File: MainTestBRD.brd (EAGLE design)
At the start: 100 x 80 mm, 24 parts, among them J1 COMPUTER-PERIPHERAL-POWERVERT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, U1 ATMEGA128-SMD

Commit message: intermedate variant
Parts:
- R1, R2: value (none) -> 1.8k; device mbed-rlcq:0.125W -> SparkFun-Resistors:0603-RES
- moved R2 10.2 mm to (86.4, 71.1), turned to 180 degrees
- moved LED2 10.2 mm to (95.2, 71.1)
- flipped J1 to the bottom
- turned R1 to 180 degrees
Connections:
- net N$13 renamed RESET
- net LED1: now also R1.2; no longer R1.P$1
- net LED2: now also R2.2; no longer R2.P$1
- net N$2: now also R2.1; no longer R2.P$2
- net N$5: now also R1.1; no longer R1.P$2
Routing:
- net VCC: track 184.7 -> 30.6 mm
- net GND: track 287.3 -> 240.2 mm
- net PF6: track 22.5 -> 0.00 mm
- net PF4: track 22.5 -> 0.00 mm
- net PF5: track 17.4 -> 0.00 mm
- net LED2: track 37.0 -> 24.7 mm
- net PF7: track 10.9 -> 0.00 mm
- net VDD: track 137.1 -> 128.7 mm
- net N$2: track 2.91 -> 6.55 mm
- net LED1: track 2.98 -> 5.47 mm
- net N$5: track 4.10 -> 6.54 mm
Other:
- board size 100 x 80 mm -> 100 x 62.2 mm

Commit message: other pinouts
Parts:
- removed J1: COMPUTER-PERIPHERAL-POWERVERTICAL, SparkFun-Connectors:COMPUTER-PERIPHERAL-POWER
- removed U$2: JTAGICE3-CONNECTOR100MIL-SMD, con-jtagice3:JTAGICE3-100MIL-SMD
- added JP1: M05X2PTH, SparkFun-Connectors:AVR_ICSP
- added U$3: JTAGICE3-CONNECTOR50MIL-THT, con-jtagice3:JTAGICE3-50MIL
- added U2: (no value), SparkFun-Connectors:USB-AB-MICRO-SMD
- moved R3 45.3 mm to (45.7, 57.1)
- moved R4 43.4 mm to (49.5, 59.7), turned to 270 degrees
- moved LED1 43.0 mm to (52.3, 67.3)
- moved LED2 42.9 mm to (52.3, 69.8)
- moved R1 39.4 mm to (47.0, 67.3)
- moved R2 39.4 mm to (47.0, 69.8)
- moved U$1 38.1 mm to (35.6, 63.5)
- moved C9 37.4 mm to (58.8, 41.2)
- moved C10 36.5 mm to (58.8, 36.4), turned to 0 degrees
- moved U1 36.4 mm to (35.6, 38.1)
- moved S1 35.9 mm to (52.1, 24.1), turned to 270 degrees
- moved Y1 35.6 mm to (51.7, 38.8)
- moved S2 35.6 mm to (20.3, 73.7)
- moved IT1 34.9 mm to (7.62, 71.1)
- moved C2 30.7 mm to (6.35, 38.1), turned to 0 degrees
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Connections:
- new net N$10: JP1.10, U1.6
- new net N$11: JP1.8, U1.5
- new net N$12: JP1.6, U1.4
- new net N$13: JP1.4, U1.3
- new net N$14: JP1.2, U1.2
- new net N$15: JP1.9, U1.7
- new net N$16: JP1.7, U1.8
- new net N$17: JP1.5, U1.9
- new net N$3: R3.1, U1.28
- net BT_RX: no longer R3.1, U1.28
- net GND: now also JP1.3, U$3.P0, U$3.P2, U2.GND; no longer J1.GND
- net PF4: now also U$3.P1; no longer U$2.1
- net PF5: now also U$3.P5; no longer U$2.5
- net PF6: now also U$3.P3; no longer U$2.3
- net PF7: now also U$3.P9; no longer U$2.9
- net VCC: now also JP1.1, U$3.P4, U2.VBUS; no longer J1.5V, U$2.4
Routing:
- net VCC: track 30.6 -> 153.8 mm
- net VDD: track 128.7 -> 89.3 mm
- net RESET: track 46.3 -> 15.7 mm
- net BT_RX: track 35.1 -> 8.97 mm
- net BT_TX: track 41.6 -> 20.4 mm
- net PF7: track 0.00 -> 20.7 mm
- net N$17: track 0.00 -> 20.0 mm
- net N$3: track 0.00 -> 18.2 mm
- net N$16: track 0.00 -> 14.9 mm
- net N$15: track 0.00 -> 9.30 mm
- net PF5: track 0.00 -> 8.82 mm
- net PF6: track 0.00 -> 8.82 mm
- net N$14: track 0.00 -> 7.15 mm
- net N$13: track 0.00 -> 6.27 mm
- net N$10: track 0.00 -> 5.97 mm
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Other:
- board size 100 x 62.2 mm -> 64.4 x 62.3 mm
- board text added: "Vcc"

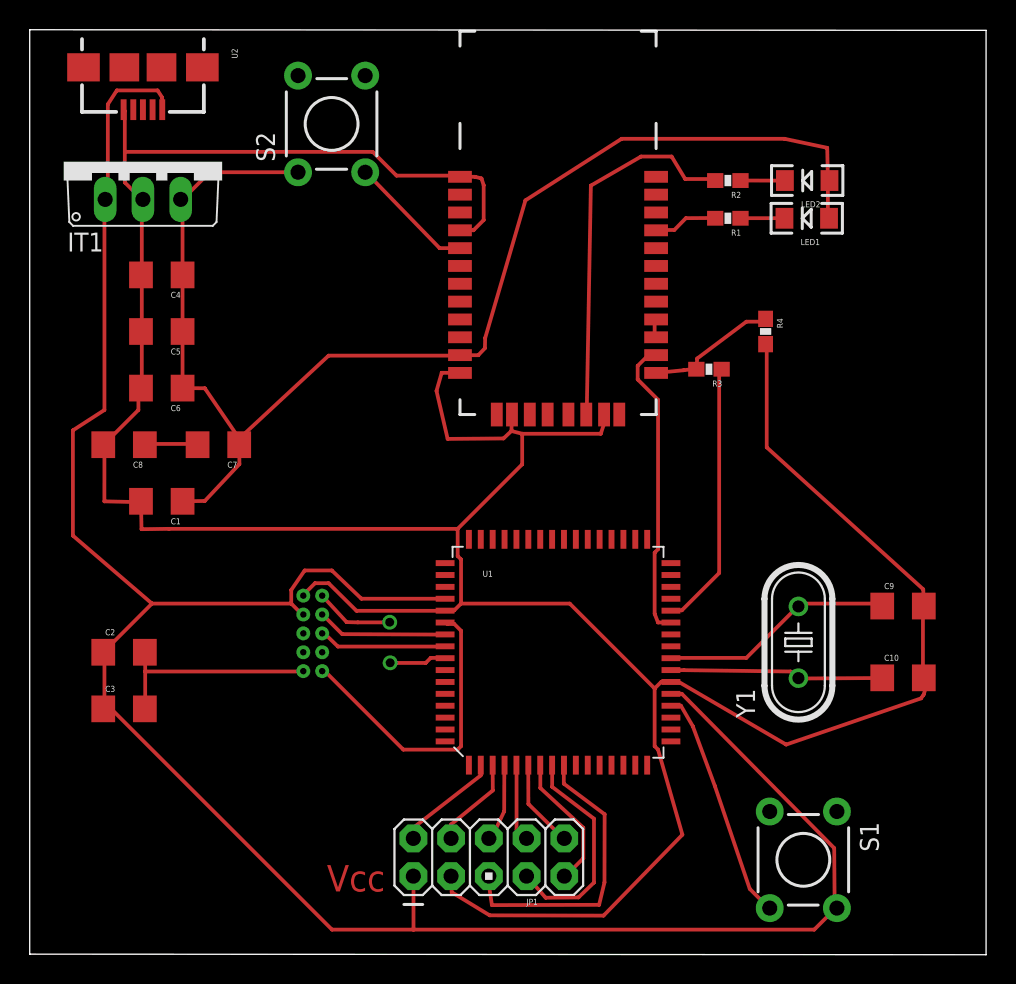
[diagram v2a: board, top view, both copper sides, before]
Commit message: additional pin outs added
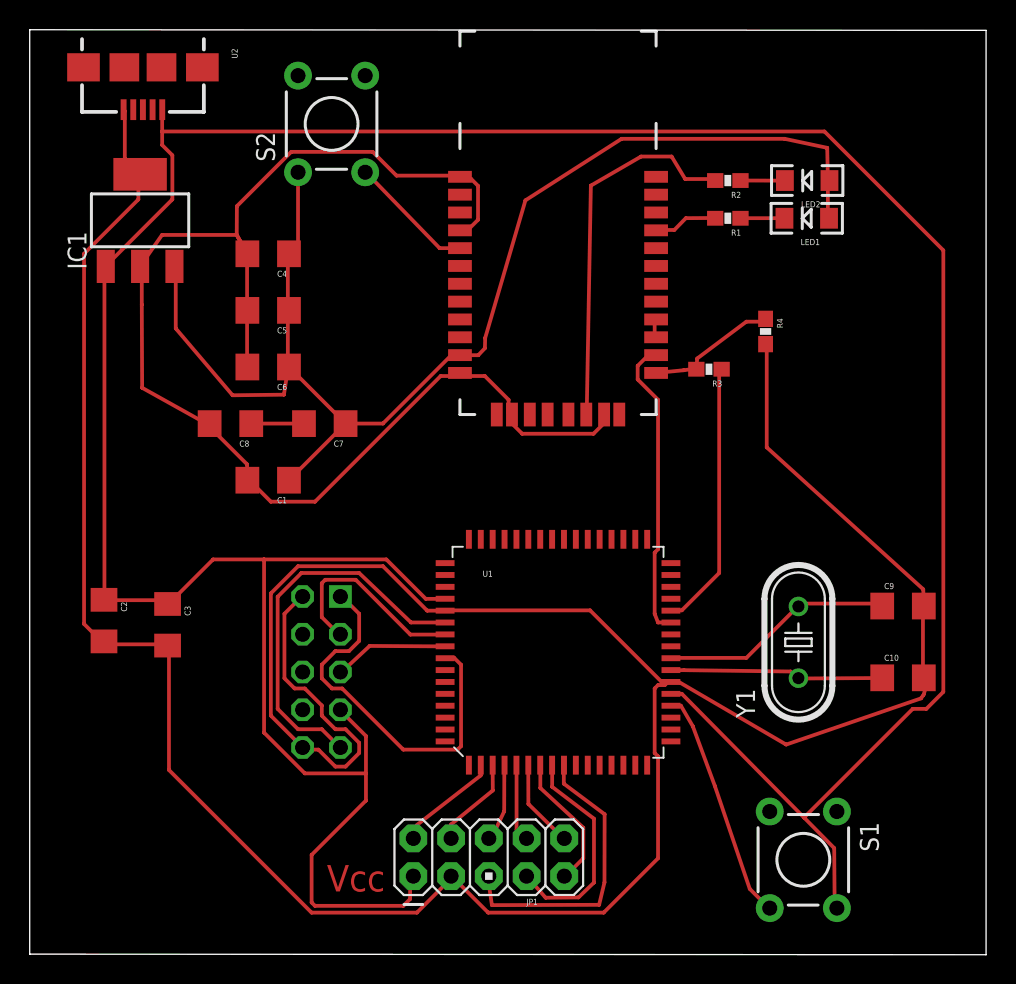
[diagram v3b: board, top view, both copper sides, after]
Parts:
- removed IT1: LM3940IT-3.3, LM3940:TO220V
- removed U$3: JTAGICE3-CONNECTOR50MIL-THT, con-jtagice3:JTAGICE3-50MIL
- added IC1: LM3940IMP-3.3, mylib:SOT223
- added JP2: AVR-JTAG-10, atmel:AVR-JTAG-10
- moved C1 7.30 mm to (16.1, 49.7)
- moved C4 7.30 mm to (16.1, 64.9)
- moved C5 7.30 mm to (16.1, 61.1)
- moved C7 7.30 mm to (19.9, 53.5)
- moved C8 7.30 mm to (13.5, 53.5)
- moved C6 7.30 mm to (16.1, 57.3)
- moved C3 6.37 mm to (9.28, 40.0), turned to 270 degrees
- moved C2 2.52 mm to (5.00, 40.2), turned to 270 degrees
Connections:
- removed net PF4: U$3.P1, U1.57
- removed net PF5: U$3.P5, U1.56
- removed net PF6: U$3.P3, U1.55
- removed net PF7: U$3.P9, U1.54
- new net AGND: C1.2, C4.2, C5.2, C6.2, C8.2, IC1.2, U$1.1, U$1.12, U$1.28, U$1.29, U$1.4
- new net N$18: JP2.3, U1.55
- new net N$19: JP2.9, U1.54
- new net N$6: JP2.1, U1.57
- new net N$9: JP2.5, U1.56
- net GND: now also IC1.4, JP2.10, JP2.2; no longer C1.2, C4.2, C5.2, C6.2, C8.2, IT1.2, U$1.1, U$1.12, U$1.28, U$1.29, U$1.4, U$3.P0, U$3.P2
- net VCC: now also IC1.1, JP2.7; no longer IT1.1, U$3.P4
- net VDD: now also IC1.3; no longer IT1.3
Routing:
- net AGND: track 0.00 -> 92.5 mm
- net VCC: track 153.8 -> 222.0 mm
- net N$19: track 0.00 -> 26.5 mm
- net N$6: track 0.00 -> 25.9 mm, vias 1 -> 0
- net GND: track 235.1 -> 212.5 mm
- net PF7: track 20.7 -> 0.00 mm
- net N$18: track 0.00 -> 13.9 mm
- net PF5: track 8.82 -> 0.00 mm
- net PF6: track 8.82 -> 0.00 mm
- net N$9: track 0.00 -> 7.73 mm, vias 1 -> 0
- net PF4: track 5.29 -> 0.00 mm
- net N$7: track 3.72 -> 0.00 mm
- net VDD: track 89.3 -> 88.1 mm

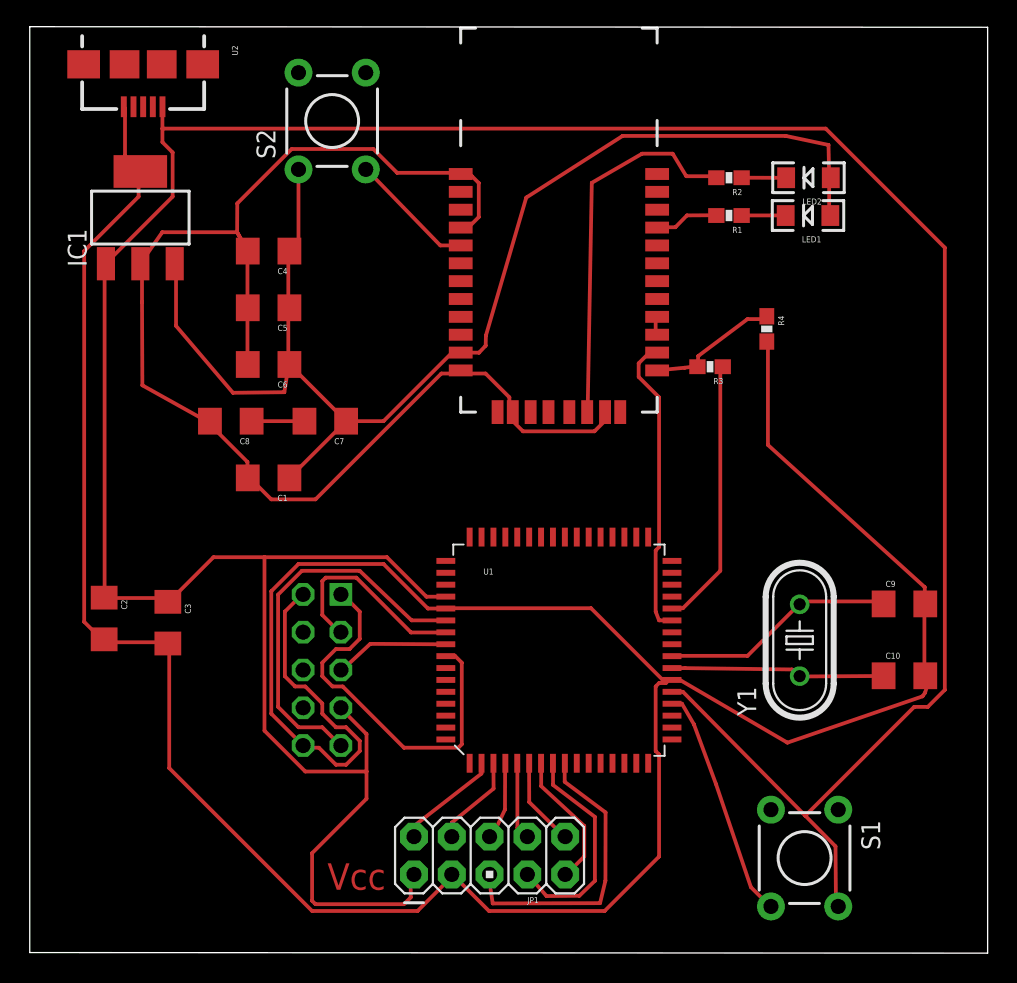
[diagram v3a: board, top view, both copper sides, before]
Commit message: new power led
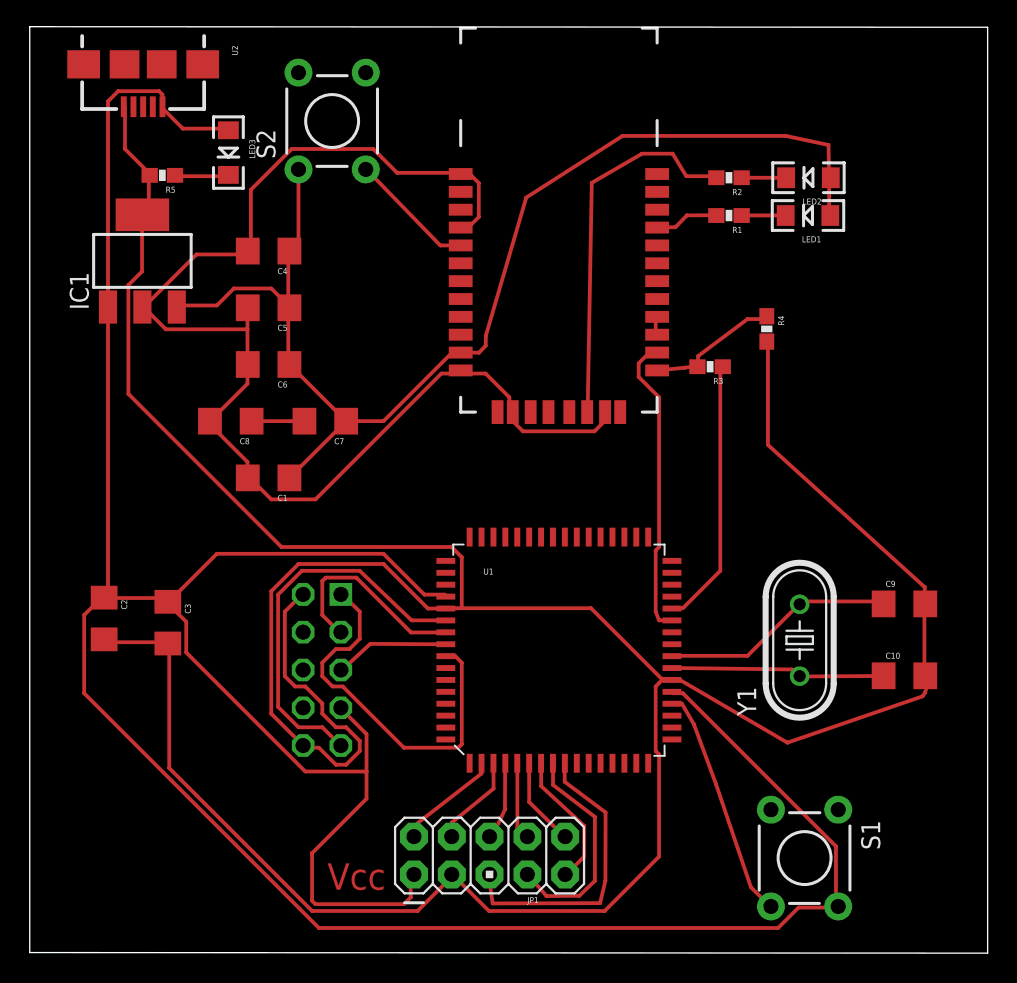
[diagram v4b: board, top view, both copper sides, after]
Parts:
- added LED3: (no value), SparkFun-LED:LED-1206
- added R5: 1.8k, SparkFun-Resistors:0603-RES
- moved IC1 2.91 mm to (3.76, 60.5)
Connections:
- new net N$20: LED3.C, R5.1
- net GND: now also R5.2
- net VCC: now also LED3.A
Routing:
- net VCC: track 222.0 -> 196.6 mm
- net GND: track 212.5 -> 225.1 mm
- net VDD: track 88.1 -> 81.0 mm
- net AGND: track 92.5 -> 87.1 mm
- net N$20: track 0.00 -> 3.65 mm

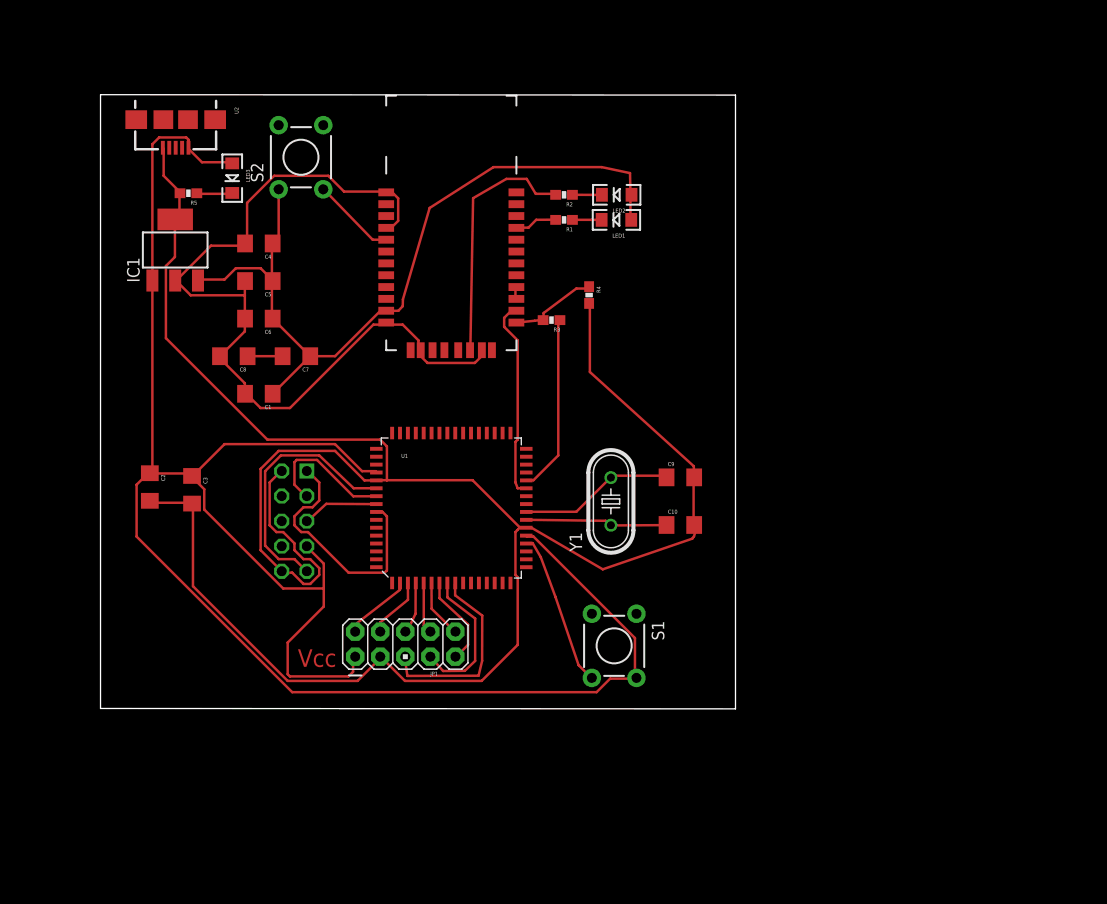
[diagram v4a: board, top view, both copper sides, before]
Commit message: new usb connector
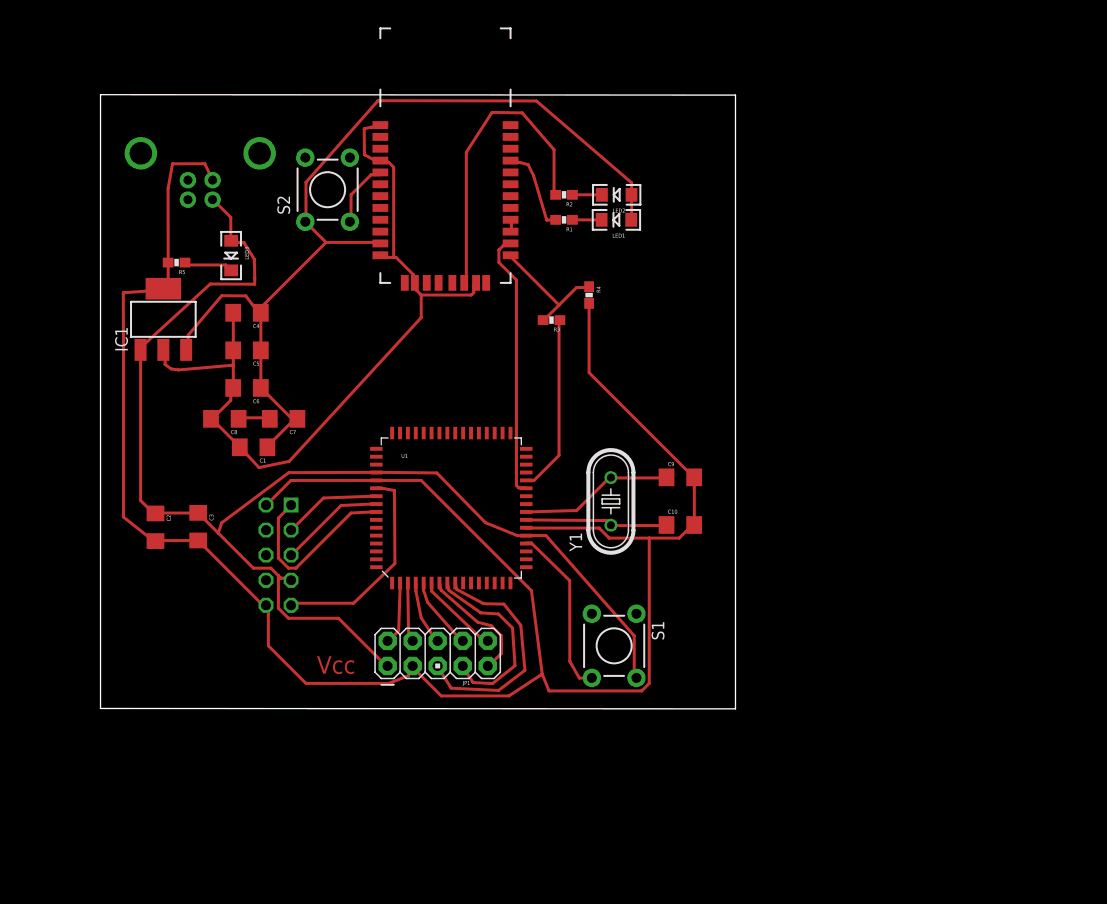
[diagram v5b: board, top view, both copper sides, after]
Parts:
- removed U2: (no value), SparkFun-Connectors:USB-AB-MICRO-SMD
- added JP4: USB-B, SparkFun-Connectors:USB-B-PTH
- moved LED3 7.85 mm to (13.2, 63.7)
- moved R5 7.13 mm to (7.71, 63.0)
- moved C4 7.13 mm to (14.8, 57.9)
- moved C5 7.13 mm to (14.8, 54.1)
- moved IC1 7.13 mm to (2.56, 53.4)
- moved C6 7.13 mm to (14.8, 50.3)
- moved U$1 6.85 mm to (35.0, 70.3)
- moved C7 6.48 mm to (18.6, 47.1)
- moved C8 6.41 mm to (12.6, 47.1)
- moved C1 5.45 mm to (15.5, 44.3)
- moved S2 4.26 mm to (23.0, 70.4)
- moved C2 4.12 mm to (5.57, 36.1)
- moved JP2 3.80 mm to (18.1, 33.3)
- moved C3 3.79 mm to (9.90, 36.2)
- moved JP1 3.41 mm to (34.2, 23.4)
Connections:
- net GND: now also JP4.GND; no longer U2.GND
- net VCC: now also JP4.VBUS; no longer U2.VBUS
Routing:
- net VCC: track 196.6 -> 131.9 mm
- net VDD: track 81.0 -> 94.7 mm
- net GND: track 225.1 -> 212.6 mm
- net N$6: track 25.9 -> 18.6 mm
- net BT_TX: track 20.4 -> 27.2 mm
- net LED2: track 25.2 -> 31.0 mm
- net N$19: track 26.5 -> 21.5 mm
- net LED1: track 4.32 -> 8.76 mm
- net N$16: track 14.9 -> 19.3 mm
- net AGND: track 87.1 -> 82.8 mm
- net BT_RX: track 8.97 -> 13.2 mm
- net N$17: track 20.0 -> 24.0 mm
- net N$18: track 13.9 -> 9.98 mm
- net N$15: track 9.30 -> 12.3 mm
- net N$9: track 7.73 -> 10.7 mm
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
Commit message: __
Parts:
- moved C1 16.5 mm to (28.6, 54.3), turned to 270 degrees
- moved C8 13.8 mm to (25.7, 51.3), turned to 270 degrees
- moved C7 12.4 mm to (25.7, 57.3), turned to 270 degrees
- moved C6 8.41 mm to (22.6, 53.6), turned to 270 degrees
- moved C4 4.30 mm to (15.0, 53.6), turned to 270 degrees
- moved C5 3.95 mm to (18.8, 53.6), turned to 270 degrees
- moved S2 1.17 mm to (22.0, 71.0)
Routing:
- net VCC: track 131.9 -> 181.9 mm, vias 0 -> 3
- net AGND: track 82.8 -> 68.7 mm
- net N$15: track 12.3 -> 0.00 mm
- net N$10: track 8.78 -> 0.00 mm
- net VDD: track 94.7 -> 87.2 mm
- net N$6: track 18.6 -> 12.0 mm, vias 0 -> 1
- net N$17: track 24.0 -> 20.5 mm
- net N$16: track 19.3 -> 16.9 mm
- net GND: track 212.6 -> 214.6 mm
- net LED2: track 31.0 -> 30.0 mm
- net N$19: track 21.5 -> 20.8 mm
- net RESET: track 17.4 -> 16.8 mm
- net BT_TX: track 27.2 -> 27.7 mm
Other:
- board size 64.4 x 62.3 mm -> 77.5 x 74.9 mm
- board text removed: "Vcc"
